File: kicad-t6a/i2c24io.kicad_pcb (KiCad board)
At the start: 2 copper layers, 62.6 x 21.7 mm, 90 parts, among them J1 PMOD_02x06, J2 PMOD_02x06, J3 Conn_01x14, J4 Conn_01x12, SW1 SW_DIP_x03, U1 TCA6424A

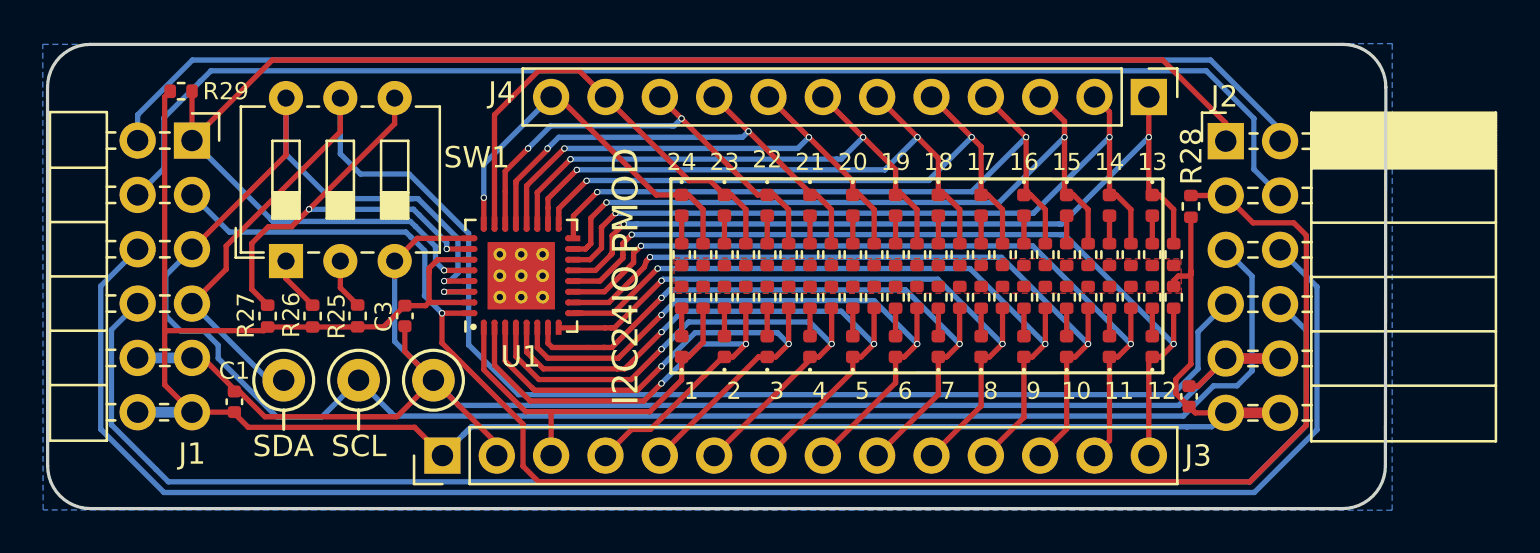
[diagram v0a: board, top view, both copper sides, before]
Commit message: KiCad v7 upgrade and GCC v10 fix
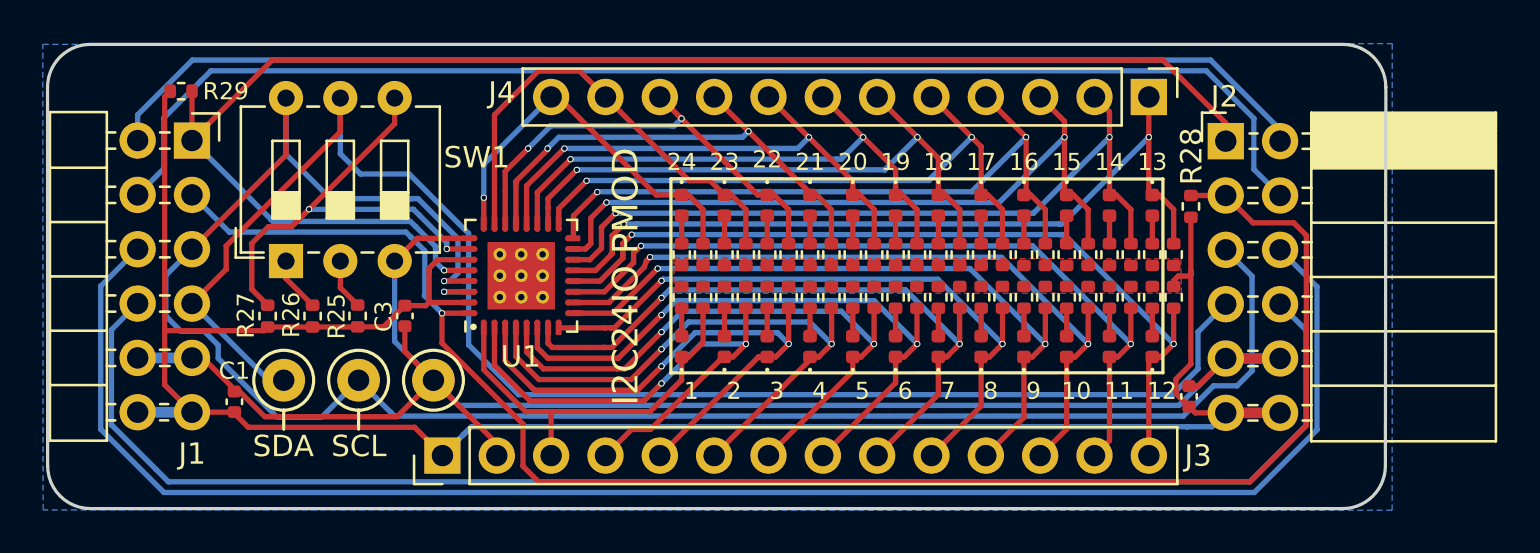
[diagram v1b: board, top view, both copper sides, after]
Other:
- net class 0.25 SMD removed
- net class Default removed
